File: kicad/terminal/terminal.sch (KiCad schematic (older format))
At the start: 36 parts, among them J1 USB, J2 PS2, J3 VGA, J4 Composite, J5 Serial, J6 External 5V, J7 ICSP, U1 PIC32MX250F128B-I_SP, U2 MCP1700-3302E_TO92, Y1 8MHz

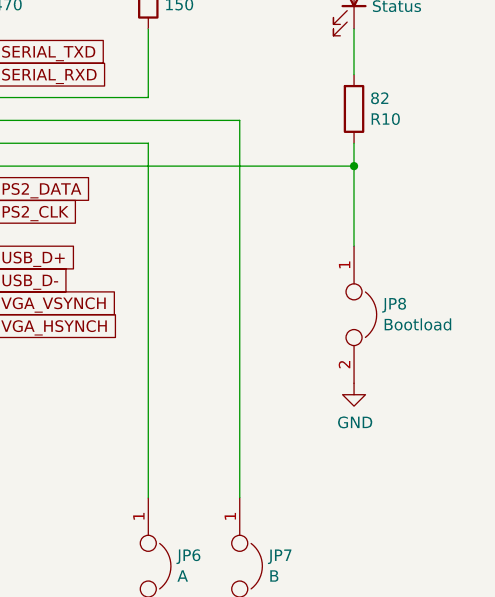
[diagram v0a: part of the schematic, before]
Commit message: Use oval holes instead of cuts in footprints. Remove bootload jumper.
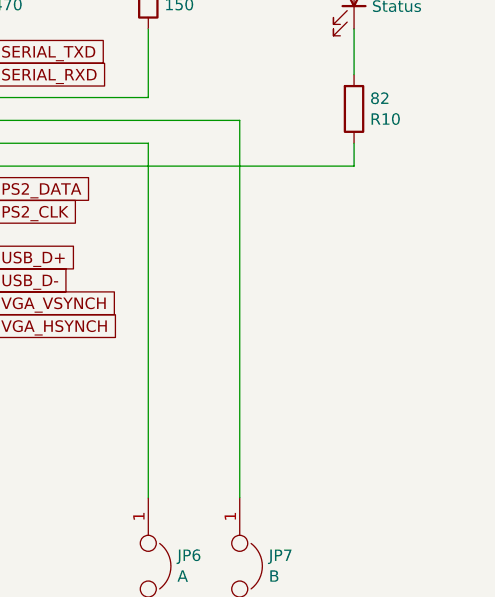
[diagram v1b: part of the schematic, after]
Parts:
- removed JP8: Bootload, Connector_PinHeader_2.54mm:PinHeader_1x02_P2.54mm_Vertical, symbol Device:Jumper
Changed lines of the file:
@@
 	5750 3050 5850 3050
-$Comp
-L Device:Jumper JP8
-U 1 1 5D71D6EC
-P 10000 3250
-F 0 "JP8" V 9954 3377 50  0000 L CNN
-F 1 "Bootload" V 10045 3377 50  0000 L CNN
-F 2 "Connector_PinHeader_2.54mm:PinHeader_1x02_P2.54mm_Vertical" H 10000 3250 50  0001 C CNN
-F 3 "~" H 10000 3250 50  0001 C CNN
-	1    10000 3250
-	0    1    1    0
-$EndComp
-$Comp
-L power:GND #PWR0119
-U 1 1 5D71DF6E
-P 10000 3550
-F 0 "#PWR0119" H 10000 3300 50  0001 C CNN
-F 1 "GND" H 10005 3377 50  0000 C CNN
-F 2 "" H 10000 3550 50  0001 C CNN
-F 3 "" H 10000 3550 50  0001 C CNN
-	1    10000 3550
-	1    0    0    -1
-$EndComp
 $Comp
 L Device:Jumper JP4
@@
 	9100 4650 9100 4800
 Wire Wire Line
-	10000 2600 10000 2950
-Connection ~ 10000 2600
-Wire Wire Line
 	9100 1200 9100 1650

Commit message: VGA hardware
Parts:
- removed J4: Composite, terminal:SWITCHCRAFT_PJRAN1X1U01X, symbol Connector:Barrel_Jack_Switch
- removed JP5: C, Connector_PinHeader_2.54mm:PinHeader_1x02_P2.54mm_Vertical, symbol Device:Jumper
- removed JP6: A, Connector_PinHeader_2.54mm:PinHeader_1x02_P2.54mm_Vertical, symbol Device:Jumper
- removed JP7: B, Connector_PinHeader_2.54mm:PinHeader_1x02_P2.54mm_Vertical, symbol Device:Jumper
- removed R8: 470, Resistor_THT:R_Axial_DIN0207_L6.3mm_D2.5mm_P7.62mm_Horizontal, symbol Device:R
- removed R9: 150, Resistor_THT:R_Axial_DIN0207_L6.3mm_D2.5mm_P7.62mm_Horizontal, symbol Device:R
- U1: value PIC32MX250F128B-I_SP -> PIC32MX270F256B-I_SP; symbol terminal:PIC32MX250F128B-I_SP -> terminal:PIC32MX270F256B-I_SP
- Y1: value 8MHz -> 10MHz
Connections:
- no-connect marks 11 -> 13
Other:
- moved on the sheet: C1, C2, C3, C4, C5, C6, C7, D1, J1, J2, J3, J5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

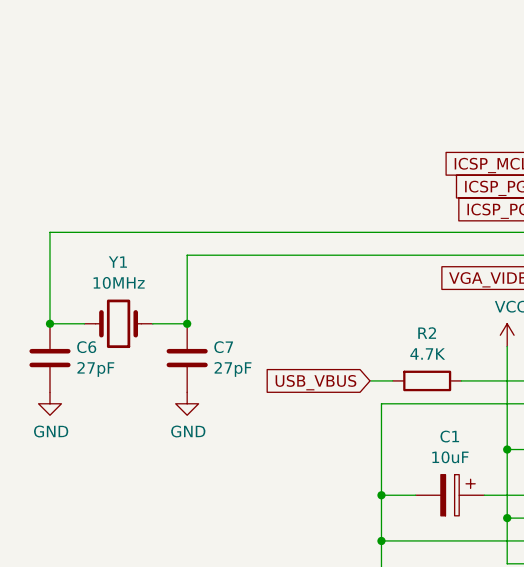
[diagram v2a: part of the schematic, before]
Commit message: Adjust crystal value in schematics and PCB
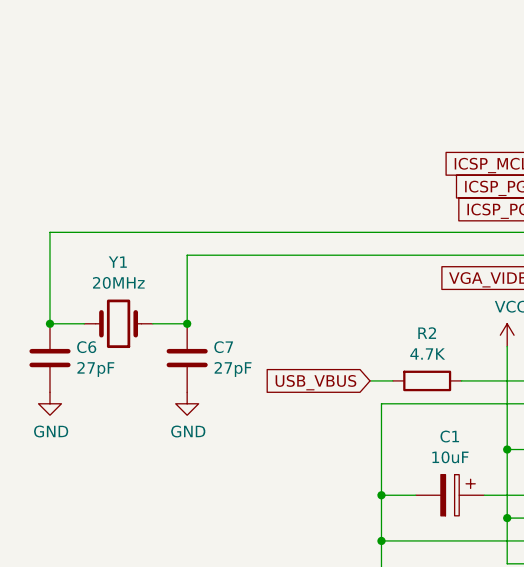
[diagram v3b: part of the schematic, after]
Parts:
- Y1: value 10MHz -> 20MHz
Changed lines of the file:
@@
 P 1250 2250
 F 0 "Y1" H 1250 1982 50  0000 C CNN
-F 1 "10MHz" H 1250 2073 50  0000 C CNN
+F 1 "20MHz" H 1250 2073 50  0000 C CNN
 F 2 "Crystal:Crystal_HC49-U_Vertical" H 1250 2250 50  0001 C CNN
 F 3 "~" H 1250 2250 50  0001 C CNN

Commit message: Port version 3 firmware (#15)
* Port version 3 firmware

* Convert PS/2 scancode to USB HID info

* Simplified VGA driver

* One DMA transfer per frame

* Byte-aligned VGA buffer

* Monochrome configuration

* Constant luminance table

* Yield to probe keyboard

* Fix keyboard LEDs

* Clear screen line for monochrome

* Use local buffer for echo mode

* Fix SD/SU

* Probe keyboard when in config UI

* Optimize character rendering

* Terminus bold and normal fonts. Write config to NVM. Config for flow control and inverted serial. Fix CHA.

* Start-up message

* Re-use terminal keyboard driver for config UI

* Non-polarized C1, C2 and C3

* IBM PC charset. HPR, VPR, REP, CHT, CBT controls. Separate receive and transmit C1 modes.

* Fix line-wrapping semantics according DEC STD-070 with wraptest

* Fix color adjustments when rendering character

* Handle secondary DA and DECSTR

* Adjust F1-F4 codes

* Support 30 rows mode to use full VGA resolution

* Shift-Alt-Ctrl modifiers

* Configurable monochrome transformation

* Alternative cells

* OC4 to generate optimal SPI framing. Remove support for screen buffer padding.

* Adjust config UI copy

* Clear screen when alternative cells are not supported

* 4K UART receive buffer

* Hardware changes for optimal SPI framing

* Keyboard compatibility: PC/Sun and VT220

* Externalize tab stops and cells memory. Use bitset for tab stops.

* Keypad mode and keyboard led initialization

* Fix setting initial keyboard LEDs

* Process PS/2 keyboard command response. Detect keyboard.

* 3.0
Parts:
- C1, C2, C3: footprint Capacitor_THT:CP_Radial_Tantal_D5.0mm_P5.00mm -> Capacitor_THT:C_Disc_D5.0mm_W2.5mm_P5.00mm; symbol Device:CP -> Device:C
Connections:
- net VGA_HSYNCH: no longer U1.18 (TDO/RPB9/SDA1/CTED4/PMD3/RB9)
- net at U1.6 (AN4/C1INB/C2IND/RPB2/SDA2/CTED13/PMD2/RB2): now also U1.18 (TDO/RPB9/SDA1/CTED4/PMD3/RB9)
- no-connect marks 13 -> 12
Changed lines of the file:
@@
 EESchema Schematic File Version 4
-LIBS:terminal-cache
 EELAYER 30 0
 EELAYER END
@@
 	2950 2800 2950 2350
 $Comp
-L Device:CP C1
+L Device:C C1
 U 1 1 5D61AF5F
 P 2700 3000
 F 0 "C1" V 2445 3000 50  0000 C CNN
 F 1 "10uF" V 2536 3000 50  0000 C CNN
-F 2 "Capacitor_THT:CP_Radial_Tantal_D5.0mm_P5.00mm" H 2738 2850 50  0001 C CNN
+F 2 "Capacitor_THT:C_Disc_D5.0mm_W2.5mm_P5.00mm" H 2738 2850 50  0001 C CNN
 F 3 "~" H 2700 3000 50  0001 C CNN
 	1    2700 3000
@@
 $EndComp
 $Comp
-L Device:CP C2
+L Device:C C2
 U 1 1 5D61D25D
 P 2050 7400
 F 0 "C2" H 2168 7446 50  0000 L CNN
 F 1 "10uF" H 2168 7355 50  0000 L CNN
-F 2 "Capacitor_THT:CP_Radial_Tantal_D5.0mm_P5.00mm" H 2088 7250 50  0001 C CNN
+F 2 "Capacitor_THT:C_Disc_D5.0mm_W2.5mm_P5.00mm" H 2088 7250 50  0001 C CNN
 F 3 "~" H 2050 7400 50  0001 C CNN
 	1    2050 7400
@@
 $EndComp
 $Comp
-L Device:CP C3
+L Device:C C3
 U 1 1 5D61E642
 P 900 7400
 F 0 "C3" H 1018 7446 50  0000 L CNN
 F 1 "10uF" H 1018 7355 50  0000 L CNN
-F 2 "Capacitor_THT:CP_Radial_Tantal_D5.0mm_P5.00mm" H 938 7250 50  0001 C CNN
+F 2 "Capacitor_THT:C_Disc_D5.0mm_W2.5mm_P5.00mm" H 938 7250 50  0001 C CNN
 F 3 "~" H 900 7400 50  0001 C CNN
 	1    900  7400
@@
 VGA_HSYNCH
 Wire Wire Line
-	8950 2900 9050 2900
-Wire Wire Line
-	9050 2900 9050 2500
-Wire Wire Line
 	9050 2500 8950 2500
-Connection ~ 9050 2900
-Wire Wire Line
-	9050 2900 9100 2900
 $Comp
 L Device:R R1
@@
 Wire Wire Line
 	9550 4850 9650 4850
-NoConn ~ 8950 1900
 Wire Wire Line
 	3150 1750 3550 1750
@@
 Wire Wire Line
 	8950 2200 9750 2200
+Wire Wire Line
+	8950 2900 9100 2900
+Wire Wire Line
+	9050 2500 9050 1900
+Wire Wire Line
+	9050 1900 8950 1900
 $EndSCHEMATC
